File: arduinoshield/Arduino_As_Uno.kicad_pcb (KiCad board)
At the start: 2 copper layers, 68.6 x 53.3 mm, 25 parts, among them J1 Conn_01x08, P1 Power, P2 Analog, P3 Digital, P4 Digital, P5 CONN_01X01, P6 CONN_01X01, P7 CONN_01X01, P8 CONN_01X01, U1 LM7815ACT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

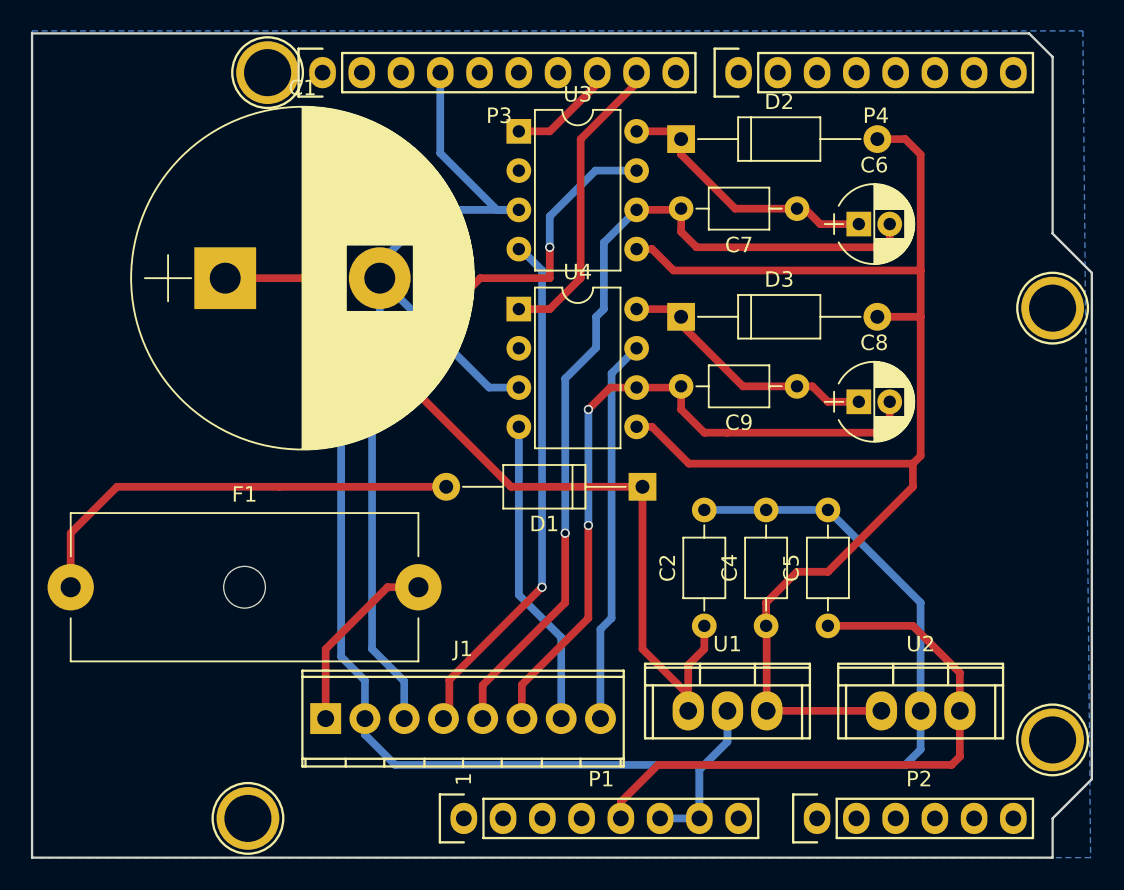
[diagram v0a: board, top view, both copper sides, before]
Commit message: redesigned arduino shield for with connectors and smd parts
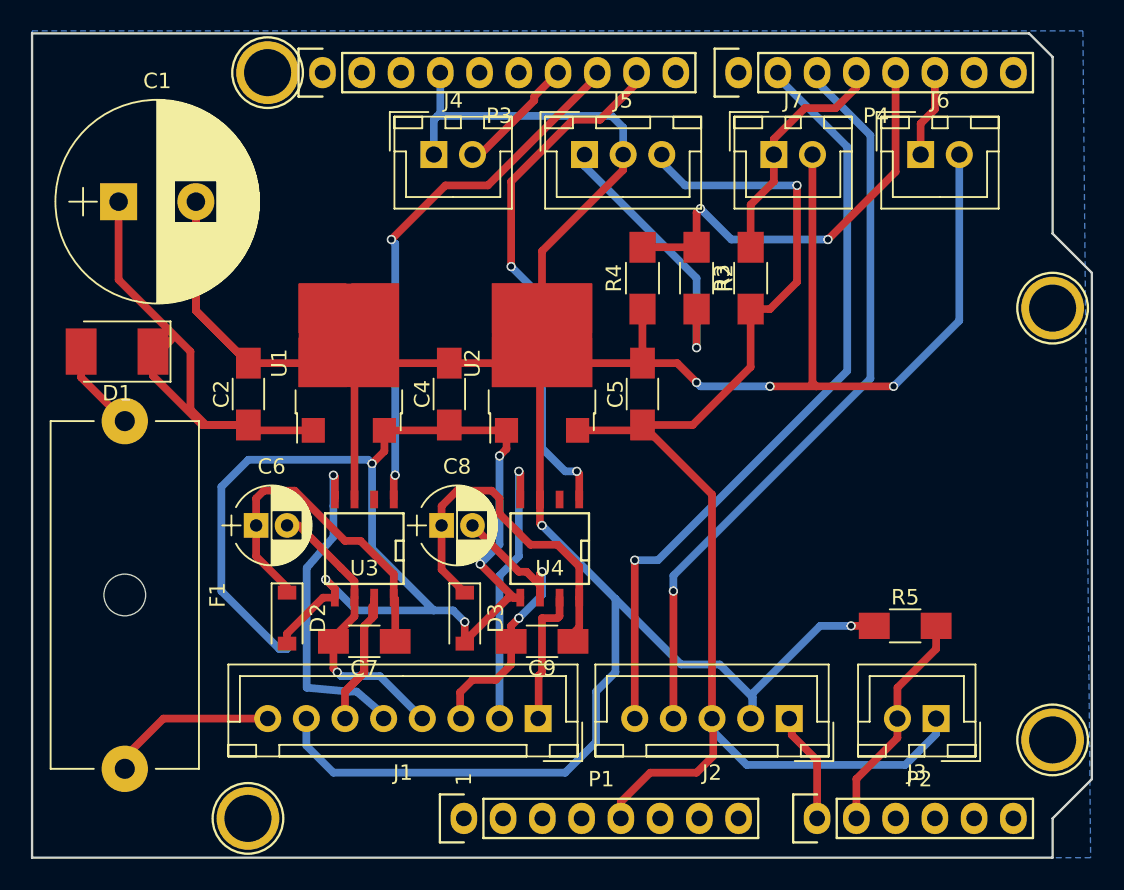
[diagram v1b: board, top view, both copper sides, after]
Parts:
- added J2: Conn_01x05, Connectors_JST:JST_XH_B05B-XH-A_05x2.50mm_Straight, F.Cu at (160.0, 117.4)
- added J3: Conn_01x02, Connectors_JST:JST_XH_B02B-XH-A_02x2.50mm_Straight, F.Cu at (169.5, 117.4)
- added J4: Conn_01x02, Connectors_JST:JST_XH_B02B-XH-A_02x2.50mm_Straight, F.Cu at (137.0, 80.9)
- added J5: Conn_01x03, Connectors_JST:JST_XH_B03B-XH-A_03x2.50mm_Straight, F.Cu at (146.7, 80.9)
- added J6: Conn_01x02, Connectors_JST:JST_XH_B02B-XH-A_02x2.50mm_Straight, F.Cu at (168.5, 80.9)
- added J7: Conn_01x02, Connectors_JST:JST_XH_B02B-XH-A_02x2.50mm_Straight, F.Cu at (159.0, 80.9)
- added R2: 10K, Resistors_SMD:R_1206_HandSoldering, F.Cu at (154.0, 88.9)
- added R3: 4K7, Resistors_SMD:R_1206_HandSoldering, F.Cu at (157.5, 88.9)
- added R4: 10K, Resistors_SMD:R_1206_HandSoldering, F.Cu at (150.5, 88.9)
- added R5: 10K, Resistors_SMD:R_1206_HandSoldering, F.Cu at (167.5, 111.4)
- C1: footprint Capacitors_THT:CP_Radial_D22.0mm_P10.00mm_SnapIn -> Capacitors_THT:CP_Radial_D13.0mm_P5.00mm
- C2, C4, C5, C7, C9: footprint Capacitors_THT:C_Axial_L3.8mm_D2.6mm_P7.50mm_Horizontal -> Capacitors_SMD:C_1206_HandSoldering
- D1: value 1N4007 -> MRA4007T3G; footprint Diodes_THT:D_A-405_P12.70mm_Horizontal -> Diodes_SMD:D_2114
- D2, D3: value 1N5819 -> 1N5819HW-7-F; footprint Diodes_THT:D_A-405_P12.70mm_Horizontal -> Diodes_SMD:D_SOD-123
- J1: footprint Connectors_Terminal_Blocks:TerminalBlock_Pheonix_MPT-2.54mm_8pol -> Connectors_JST:JST_XH_B08B-XH-A_08x2.50mm_Straight
- U1: value LM7815ACT -> MC7815BD2TR4G; footprint Power_Integrations:TO-220 -> TO_SOT_Packages_SMD:ATPAK-2
- U2: value L7805 -> L7805CD2T-TR; footprint Power_Integrations:TO-220 -> TO_SOT_Packages_SMD:ATPAK-2
- U3, U4: value IR2184 -> IR2184SPBF; footprint Housings_DIP:DIP-8_W7.62mm -> SMD_Packages:SOIC-8-N
- moved C6 43.6 mm to (125.5, 104.9)
- moved D2 40.1 mm to (127.5, 110.9), turned to 270 degrees
- moved C7 39.6 mm to (132.5, 112.4)
- moved D1 35.1 mm to (116.5, 93.6)
- moved U1 33.3 mm to (131.5, 94.4), turned to 90 degrees
- moved U2 33.3 mm to (144.0, 94.4), turned to 90 degrees
- moved C2 33.1 mm to (125.0, 96.4)
- moved U3 28.8 mm to (132.5, 106.4), turned to 180 degrees
- moved C8 28.2 mm to (137.5, 104.9)
- moved C4 25.4 mm to (138.0, 96.4)
- moved D3 24.0 mm to (139.0, 110.9), turned to 270 degrees
- moved C9 23.3 mm to (144.0, 112.4)
- moved C5 19.2 mm to (150.5, 96.4)
- moved U4 15.6 mm to (144.5, 106.4), turned to 180 degrees
- moved J1 13.8 mm to (143.7, 117.4), turned to 180 degrees
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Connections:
- J1 pad 1: Net-(F1-Pad2) -> Net-(J1-Pad1)
- J1 pad 2: GND -> Net-(J1-Pad2)
- J1 pad 3: Net-(J1-Pad3) -> Net-(C8-Pad2)
- J1 pad 4: Net-(J1-Pad4) -> Net-(C6-Pad2)
- J1 pad 5: Net-(C6-Pad2) -> Net-(J1-Pad5)
- J1 pad 6: Net-(C8-Pad2) -> Net-(J1-Pad6)
- J1 pad 7: Net-(J1-Pad7) -> GND
- J1 pad 8: Net-(J1-Pad8) -> Net-(F1-Pad2)
- P2 pad 1: (no net) -> /A0
- P2 pad 2: (no net) -> /A1
- P3 pad 7: (no net) -> /11(**/MOSI)
- P4 pad 2: (no net) -> /6(**)
- P4 pad 3: (no net) -> /5(**)
- P4 pad 4: (no net) -> /4
- P4 pad 5: (no net) -> /3(**)
- P4 pad 6: (no net) -> /2
- U3 pad 4: Net-(J1-Pad4) -> Net-(J1-Pad5)
- U3 pad 7: Net-(J1-Pad3) -> Net-(J1-Pad6)
- U4 pad 4: Net-(J1-Pad7) -> Net-(J1-Pad2)
- U4 pad 7: Net-(J1-Pad8) -> Net-(J1-Pad1)
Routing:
- net GND: track 139.8 -> 224.1 mm, vias 0 -> 5
- net /6(**): track 0.00 -> 50.2 mm, vias 0 -> 1
- net /5(**): track 0.00 -> 48.5 mm, vias 0 -> 1
- net Net-(J1-Pad3): track 47.6 -> 0.00 mm, vias 2 -> 0
- net +5V: track 39.4 -> 86.5 mm, vias 0 -> 1
- net Net-(C6-Pad2): track 56.9 -> 19.2 mm
- net Net-(J1-Pad4): track 33.7 -> 0.00 mm, vias 1 -> 0
- net /10(**/SS): track 7.07 -> 35.6 mm, vias 0 -> 2
- net /3(**): track 0.00 -> 27.8 mm, vias 0 -> 2
- net Net-(C8-Pad2): track 46.0 -> 20.3 mm
- net Net-(J1-Pad8): track 24.9 -> 0.00 mm
- net /24V-Fused: track 29.0 -> 5.67 mm
- net Net-(J1-Pad5): track 0.00 -> 21.8 mm, vias 0 -> 1
- net Net-(J1-Pad7): track 20.0 -> 0.00 mm
- net Net-(C1-Pad1): track 54.2 -> 34.4 mm
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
